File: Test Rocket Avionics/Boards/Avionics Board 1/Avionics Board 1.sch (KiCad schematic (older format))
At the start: 52 parts, among them J1 USB_A, J10 CHASSIS_GND, J11 CHASSIS_GND, J12 CHASSIS_GND, J13 CHASSIS_GND, J14 1S LiPo, J2 1S LiPo, J3 EXPANSION_HEADER, U1 ECS-.327-12.5-17X-TR, U2 SPX3819M5-L-3-3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

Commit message: Update some stuff
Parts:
- removed J3: EXPANSION_HEADER, Pin_Headers:Pin_Header_Straight_2x10_Pitch1.00mm, symbol Conn_02x11_Odd_Even
- added C20, C6: 2.2u, Capacitors_SMD:C_1206, symbol C
- added C21: 1u, Capacitors_SMD:C_0805, symbol C
- added C22: 220p, Capacitors_SMD:C_0805, symbol C
- added D6: D, Diodes_SMD:D_SOD-123F, symbol D
- added J3: EXPANSION_HEADER, Pin_Headers:Pin_Header_Straight_2x14_Pitch1.00mm, symbol Conn_02x12_Odd_Even
- added J4: USB_A, Connectors:USB_Mini-B, symbol USB_A
- added J5: SERVO, Pin_Headers:Pin_Header_Straight_1x03_Pitch2.54mm, symbol Conn_01x03
- added L1: 10u, Inductors_SMD:L_Wuerth_HCI-5040, symbol L
- added R10, R11, R17: 10k, Resistors_SMD:R_0805, symbol R
- added R18: 51k, Resistors_SMD:R_0805, symbol R
- added R19: 13.3k, Resistors_SMD:R_0805, symbol R
- added U10: NC7WZ07, TO_SOT_Packages_SMD:SOT-363_SC-70-6, symbol NC7WZ07
- added U11: LMR62014, TO_SOT_Packages_SMD:SOT-23-5, symbol LMR62014
- added U6: DS3231-SO16, Housings_SOIC:SOIC-16W_7.5x10.3mm_Pitch1.27mm, symbol DS3231-SO16
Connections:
- net labels added: 6V_SERVO_SUPPLY
- wire segments 139 -> 177
- no-connect marks 15 -> 27
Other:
- note added: "Place this USB on underside of the board"

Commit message: Connect JST connector to VBatt+ and GND nets
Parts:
- BZ1: symbol Buzzer -> Avionics-Board-1-rescue:Buzzer
- C1, C10, C11, C12, C13, C15, C16, C17, C18, C19, C2, C20, C21, C22, C3, C4, C5, C6, C7, C8, C9: symbol C -> Avionics-Board-1-rescue:C
- D1: symbol D_Schottky -> Avionics-Board-1-rescue:D_Schottky
- D2, D3, D4, D5: symbol LED -> Avionics-Board-1-rescue:LED
- D6: symbol D -> Avionics-Board-1-rescue:D
- J1, J4: symbol USB_A -> Avionics-Board-1-rescue:USB_A
- J10, J11, J12, J13: symbol Conn_01x01 -> Avionics-Board-1-rescue:Conn_01x01
- J14, J2: symbol Conn_01x02 -> Avionics-Board-1-rescue:Conn_01x02
- J3: symbol Conn_02x12_Odd_Even -> Avionics-Board-1-rescue:Conn_02x12_Odd_Even
- J5: symbol Conn_01x03 -> Avionics-Board-1-rescue:Conn_01x03
- L1: symbol L -> Avionics-Board-1-rescue:L
- R1, R10, R11, R12, R13, R14, R15, R16, R17, R18, R19, R2, R3, R4, R5, R6, R7, R8, R9: symbol R -> Avionics-Board-1-rescue:R
- U1, U8: symbol ECS-.327-12.5-17X-TR -> Avionics-Board-1-rescue:ECS-.327-12.5-17X-TR
- U10: symbol NC7WZ07 -> Avionics-Board-1-rescue:NC7WZ07
- U11: symbol LMR62014 -> Avionics-Board-1-rescue:LMR62014
- U2: symbol SPX3819M5-L-3-3 -> Avionics-Board-1-rescue:SPX3819M5-L-3-3
- U3: symbol ATSAMD21G18 -> Avionics-Board-1-rescue:ATSAMD21G18
- U4: symbol MCP73831 -> Avionics-Board-1-rescue:MCP73831
- U5: symbol MPL3115A2 -> Avionics-Board-1-rescue:MPL3115A2
- U6: symbol DS3231-SO16 -> Avionics-Board-1-rescue:DS3231-SO16
- U7: symbol BNO055 -> Avionics-Board-1-rescue:BNO055

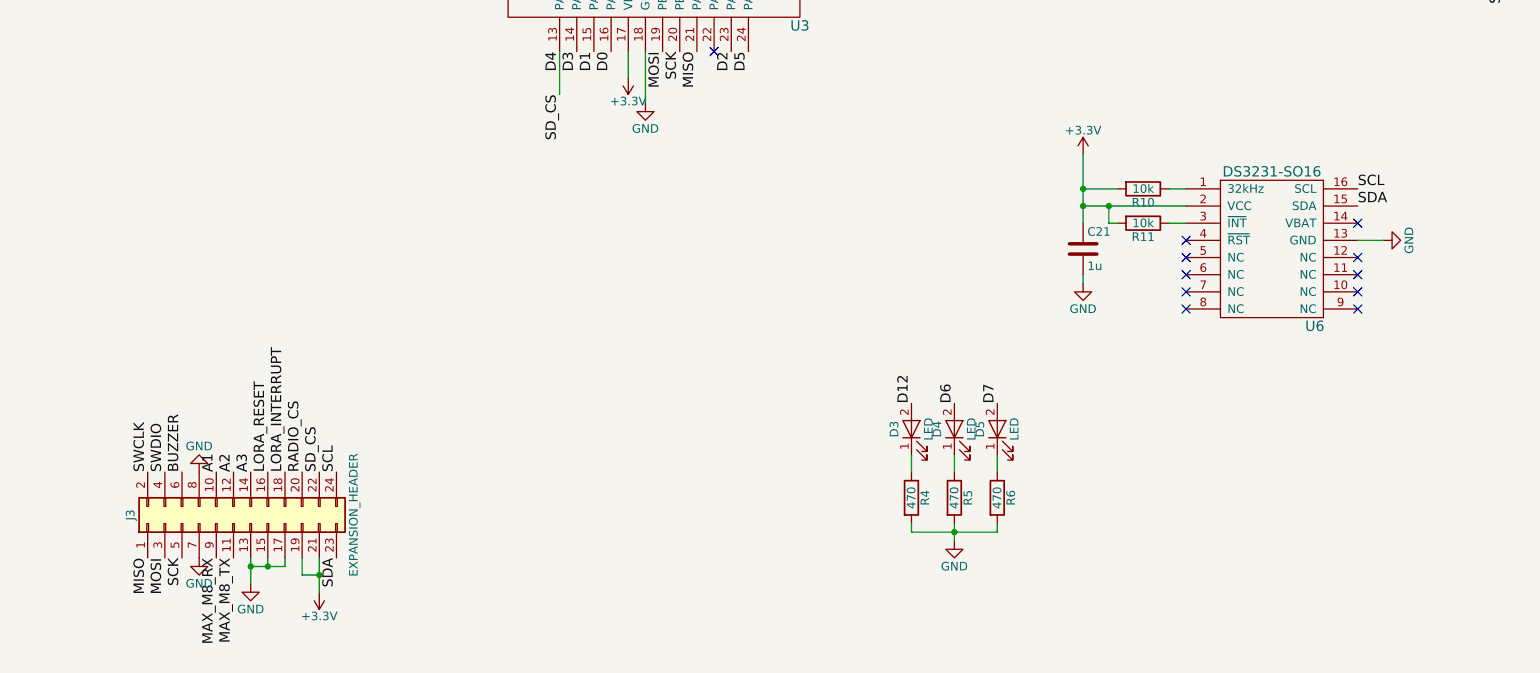
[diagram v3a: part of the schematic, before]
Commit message: Remove DS3231 and expand the J3 connector to include USB and improve pin ordering. Various bug fixes
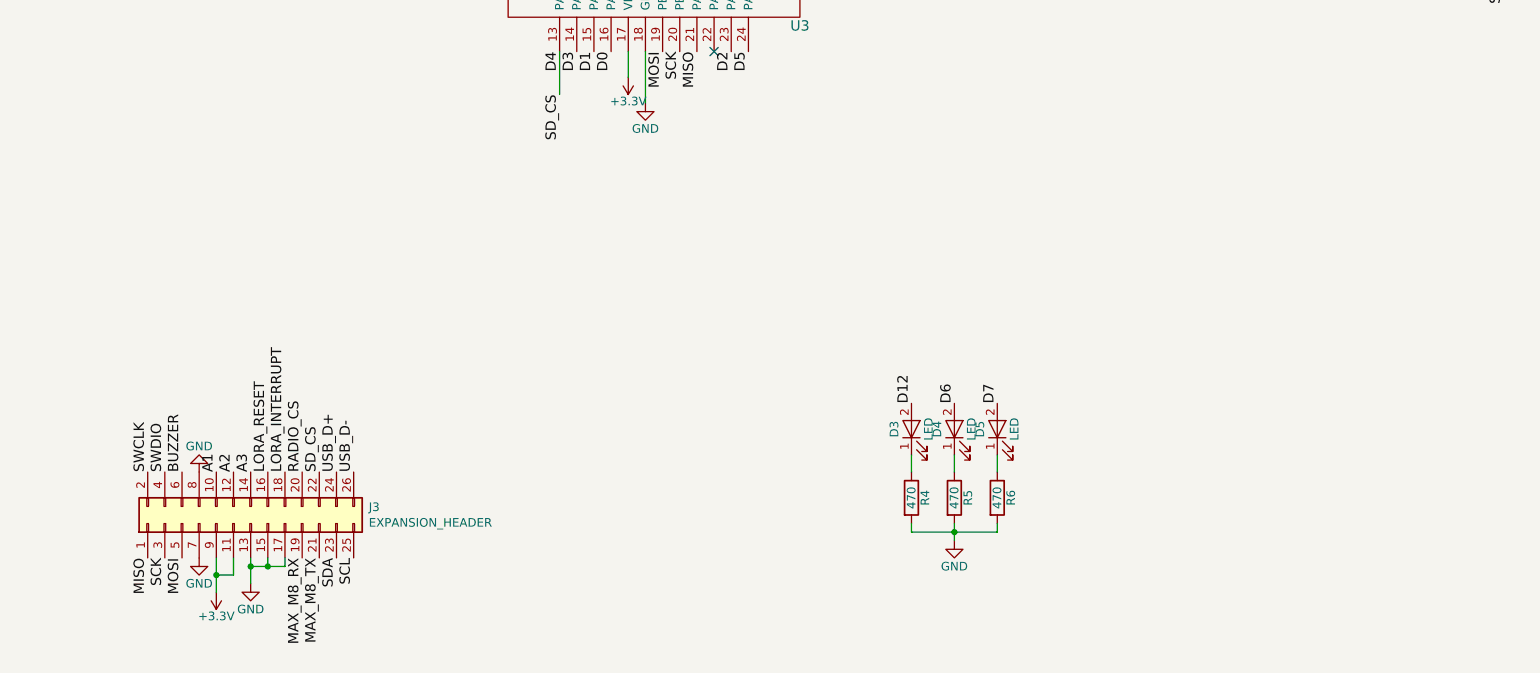
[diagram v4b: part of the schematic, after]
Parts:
- removed C21: 1u, Capacitors_SMD:C_0805, symbol Avionics-Board-1-rescue:C
- removed J3: EXPANSION_HEADER, Pin_Headers:Pin_Header_Straight_2x14_Pitch1.00mm, symbol Avionics-Board-1-rescue:Conn_02x12_Odd_Even
- removed R10, R11: 10k, Resistors_SMD:R_0805, symbol Avionics-Board-1-rescue:R
- removed U6: DS3231-SO16, Housings_SOIC:SOIC-16W_7.5x10.3mm_Pitch1.27mm, symbol Avionics-Board-1-rescue:DS3231-SO16
- added J3: EXPANSION_HEADER, Pin_Headers:Pin_Header_Straight_2x13_Pitch1.00mm, symbol Connector_Generic:Conn_02x13_Odd_Even
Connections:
- net +3V3: now also J3.11 (Pin_11), J3.9 (Pin_9)
- net A1: now also J3.10 (Pin_10)
- net A2: now also J3.12 (Pin_12)
- net A3: now also J3.14 (Pin_14)
- net A4: now also J3.16 (Pin_16)
- net A5: now also J3.6 (Pin_6)
- net D11: now also J3.21 (Pin_21)
- net D13: now also J3.19 (Pin_19)
- net D4: now also J3.22 (Pin_22)
- net D8: now also J3.18 (Pin_18)
- net D9: now also J3.20 (Pin_20)
- net GND: now also J3.13 (Pin_13), J3.15 (Pin_15), J3.17 (Pin_17), J3.7 (Pin_7), J3.8 (Pin_8)
- net MISO: now also J3.1 (Pin_1)
- net MOSI: now also J3.5 (Pin_5)
- net SCK: now also J3.3 (Pin_3)
- net SCL: now also J3.25 (Pin_25)
- net SDA: now also J3.23 (Pin_23)
- net SWCLK: now also J3.2 (Pin_2)
- net SWDIO: now also J3.4 (Pin_4)
- net USB_D+: now also J3.24 (Pin_24)
- net USB_D-: now also J3.26 (Pin_26)
- no-connect marks 27 -> 17
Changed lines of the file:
@@
 L Avionics-Board-1-rescue:+3.3V #PWR045
 U 1 1 5C4FAC8D
-P 2700 10150
-F 0 "#PWR045" H 2700 10000 50  0001 C CNN
-F 1 "+3.3V" H 2700 10290 50  0000 C CNN
-F 2 "" H 2700 10150 50  0001 C CNN
-F 3 "" H 2700 10150 50  0001 C CNN
-	1    2700 10150
+P 2100 10150
+F 0 "#PWR045" H 2100 10000 50  0001 C CNN
+F 1 "+3.3V" H 2100 10290 50  0000 C CNN
+F 2 "" H 2100 10150 50  0001 C CNN
+F 3 "" H 2100 10150 50  0001 C CNN
+	1    2100 10150
 	1    0    0    1
 $EndComp
+Text Label 1900 9950 3    60   ~ 0
+MOSI
 Text Label 1800 9950 3    60   ~ 0
-MOSI
-Text Label 1900 9950 3    60   ~ 0
 SCK
 Text Label 1700 9950 3    60   ~ 0
 MISO
-Text Label 2200 9950 3    60   ~ 0
+Text Label 2700 9950 3    60   ~ 0
 MAX_M8_TX
-Text Label 2100 9950 3    60   ~ 0
+Text Label 2600 9950 3    60   ~ 0
 MAX_M8_RX
 $Comp
@@
 SD_CS
 Wire Wire Line
-	2700 9950 2700 10050
-Wire Wire Line
-	2600 9950 2600 10050
-Wire Wire Line
-	2600 10050 2700 10050
-Connection ~ 2700 10050
-Wire Wire Line
 	2300 9950 2300 10000
 Wire Wire Line
@@
 	2500 10000 2500 9950
 Connection ~ 2400 10000
-$Comp
-L Avionics-Board-1-rescue:Conn_02x12_Odd_Even J3
-U 1 1 5C722513
-P 2200 9750
-F 0 "J3" H 2250 10350 50  0000 C CNN
-F 1 "EXPANSION_HEADER" H 2250 9050 50  0000 C CNN
-F 2 "Pin_Headers:Pin_Header_Straight_2x14_Pitch1.00mm" H 2200 9750 50  0001 C CNN
-F 3 "" H 2200 9750 50  0001 C CNN
-	1    2200 9750
-	0    -1   -1   0
-$EndComp
-Text Label 2800 9450 1    60   ~ 0
+Text Label 2900 9950 3    60   ~ 0
 SCL
 Text Label 2800 9950 3    60   ~ 0
@@
 	7100 5150 7200 5150
 Wire Wire Line
-	2700 10050 2700 10150
-Wire Wire Line
 	2300 10000 2300 10100
 Wire Wire Line
@@
 	10800 1800 10800 1850
 Wire Wire Line
-	7300 7900 7750 7900
-NoConn ~ 7750 8100
-NoConn ~ 7750 8200
-NoConn ~ 7750 8300
-NoConn ~ 7750 8400
-NoConn ~ 7750 8500
-NoConn ~ 8750 8500
-NoConn ~ 8750 8400
-NoConn ~ 8750 8300
-NoConn ~ 8750 8200
-NoConn ~ 8750 8000
-Wire Wire Line
-	8900 8100 8750 8100
-$Comp
-L Avionics-Board-1-rescue:GND #PWR063
-U 1 1 5C73A8EF
-P 8900 8100
-F 0 "#PWR063" H 8900 7850 50  0001 C CNN
-F 1 "GND" H 8900 7950 50  0000 C CNN
-F 2 "" H 8900 8100 50  0001 C CNN
-F 3 "" H 8900 8100 50  0001 C CNN
-	1    8900 8100
+	2100 10150 2100 10050
+Wire Wire Line
+	2200 9950 2200 10050
+Wire Wire Line
+	2200 10050 2100 10050
+Connection ~ 2100 10050
+Wire Wire Line
+	2100 10050 2100 9950
+$Comp
+L Connector_Generic:Conn_02x13_Odd_Even J3
+U 1 1 5CB1EFA8
+P 2300 9750
+F 0 "J3" V 2396 9062 50  0000 R CNN
+F 1 "EXPANSION_HEADER" V 2305 9062 50  0000 R CNN
+F 2 "Pin_Headers:Pin_Header_Straight_2x13_Pitch1.00mm" H 2300 9750 50  0001 C CNN
+F 3 "~" H 2300 9750 50  0001 C CNN
+	1    2300 9750
 	0    -1   -1   0
 $EndComp
-Text Label 8750 7800 0    60   ~ 0
-SCL
-Text Label 8750 7900 0    60   ~ 0
-SDA
-Wire Wire Line
-	7150 8350 7150 8300
-$Comp
-L Avionics-Board-1-rescue:GND #PWR062
-U 1 1 5C739AF9
-P 7150 8350
-F 0 "#PWR062" H 7150 8100 50  0001 C CNN
-F 1 "GND" H 7150 8200 50  0000 C CNN
-F 2 "" H 7150 8350 50  0001 C CNN
-F 3 "" H 7150 8350 50  0001 C CNN
-	1    7150 8350
-	1    0    0    -1
-$EndComp
-$Comp
-L Avionics-Board-1-rescue:C C21
-U 1 1 5C73906A
-P 7150 8150
-F 0 "C21" H 7175 8250 50  0000 L CNN
-F 1 "1u" H 7175 8050 50  0000 L CNN
-F 2 "Capacitors_SMD:C_0805" H 7188 8000 50  0001 C CNN
-F 3 "" H 7150 8150 50  0001 C CNN
-	1    7150 8150
-	1    0    0    -1
-$EndComp
-Wire Wire Line
-	7150 7800 7350 7800
-Connection ~ 7150 7800
-Wire Wire Line
-	7150 7600 7150 7800
-$Comp
-L Avionics-Board-1-rescue:+3.3V #PWR061
-U 1 1 5C738EB5
-P 7150 7600
-F 0 "#PWR061" H 7150 7450 50  0001 C CNN
-F 1 "+3.3V" H 7150 7740 50  0000 C CNN
-F 2 "" H 7150 7600 50  0001 C CNN
-F 3 "" H 7150 7600 50  0001 C CNN
-	1    7150 7600
-	1    0    0    -1
-$EndComp
-Wire Wire Line
-	7300 8000 7300 7900
-Wire Wire Line
-	7350 8000 7300 8000
-Connection ~ 7300 7900
-Wire Wire Line
-	7150 7800 7150 7900
-Wire Wire Line
-	7150 7900 7150 8000
-Connection ~ 7150 7900
-Wire Wire Line
-	7150 7900 7300 7900
-Wire Wire Line
-	7650 8000 7750 8000
-Wire Wire Line
-	7650 7800 7750 7800
-$Comp
-L Avionics-Board-1-rescue:R R11
-U 1 1 5C738866
-P 7500 8000
-F 0 "R11" V 7580 8000 50  0000 C CNN
-F 1 "10k" V 7500 8000 50  0000 C CNN
-F 2 "Resistors_SMD:R_0805" V 7430 8000 50  0001 C CNN
-F 3 "" H 7500 8000 50  0001 C CNN
-	1    7500 8000
-	0    1    1    0
-$EndComp
-$Comp
-L Avionics-Board-1-rescue:R R10
-U 1 1 5C738747
-P 7500 7800
-F 0 "R10" V 7580 7800 50  0000 C CNN
-F 1 "10k" V 7500 7800 50  0000 C CNN
-F 2 "Resistors_SMD:R_0805" V 7430 7800 50  0001 C CNN
-F 3 "" H 7500 7800 50  0001 C CNN
-	1    7500 7800
-	0    1    1    0
-$EndComp
-$Comp
-L Avionics-Board-1-rescue:DS3231-SO16 U6
-U 1 1 5C7360A0
-P 8250 8150
-F 0 "U6" H 8500 7700 60  0000 C CNN
-F 1 "DS3231-SO16" H 8250 8600 60  0000 C CNN
-F 2 "Housings_SOIC:SOIC-16W_7.5x10.3mm_Pitch1.27mm" H 8250 7450 60  0001 C CNN
-F 3 "" H 8250 7450 60  0001 C CNN
-	1    8250 8150
-	1    0    0    -1
-$EndComp
+Text Label 2800 9450 1    60   ~ 0
+USB_D+
+Text Label 2900 9450 1    60   ~ 0
+USB_D-
 $EndSCHEMATC

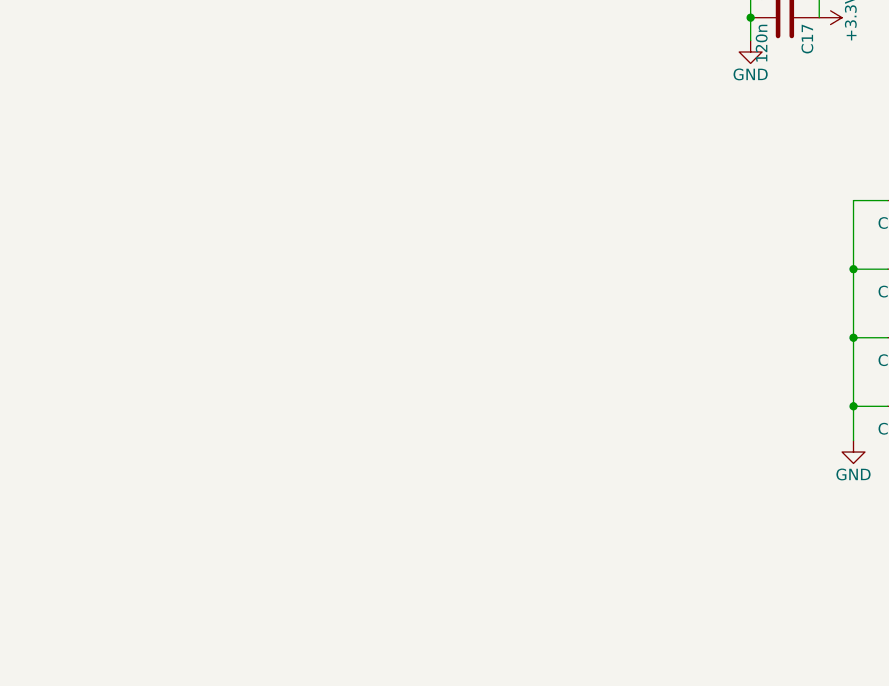
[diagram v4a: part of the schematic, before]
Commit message: Add micro SD Card, clean up ref des, power 6v boost directly from battery instead of 3.3V rail
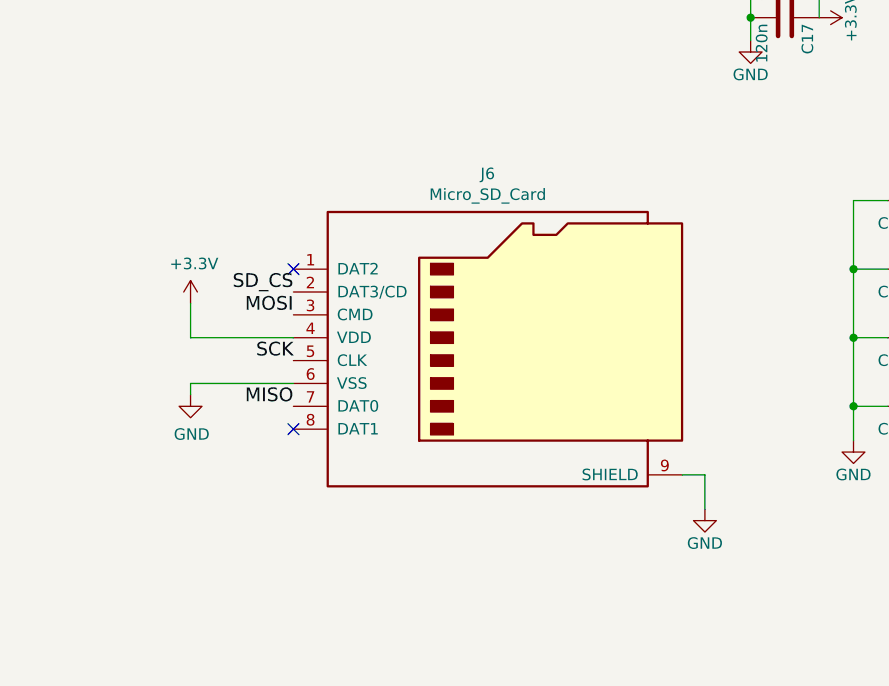
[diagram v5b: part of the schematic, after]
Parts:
- added J6: Micro_SD_Card, DannysLib:MicroSD_DM3D-SF, symbol Connector:Micro_SD_Card
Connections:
- net +3V3: now also J6.4 (VDD)
- net D4: now also J6.2 (DAT3/CD)
- net GND: now also J6.6 (VSS), J6.9 (SHIELD)
- net MISO: now also J6.7 (DAT0)
- net MOSI: now also J6.3 (CMD)
- net SCK: now also J6.5 (CLK)
- no-connect marks 17 -> 19
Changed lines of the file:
@@
 Text Label 2900 9450 1    60   ~ 0
 USB_D-
+$Comp
+L Connector:Micro_SD_Card J6
+U 1 1 5CC9B146
+P 9000 9100
+F 0 "J6" H 8950 9817 50  0000 C CNN
+F 1 "Micro_SD_Card" H 8950 9726 50  0000 C CNN
+F 2 "DannysLib:MicroSD_DM3D-SF" H 10150 9400 50  0001 C CNN
+F 3 "http://katalog.we-online.de/em/datasheet/693072010801.pdf" H 9000 9100 50  0001 C CNN
+	1    9000 9100
+	1    0    0    -1
+$EndComp
+NoConn ~ 8100 8800
+NoConn ~ 8100 9500
+Text Label 8100 9400 2    60   ~ 0
+MISO
+Text Label 8100 9000 2    60   ~ 0
+MOSI
+Text Label 8100 8900 2    60   ~ 0
+SD_CS
+Text Label 8100 9200 2    60   ~ 0
+SCK
+$Comp
+L Avionics-Board-1-rescue:+3.3V #PWR061
+U 1 1 5CCC4D2C
+P 7650 8950
+F 0 "#PWR061" H 7650 8800 50  0001 C CNN
+F 1 "+3.3V" H 7665 9123 50  0000 C CNN
+F 2 "" H 7650 8950 50  0001 C CNN
+F 3 "" H 7650 8950 50  0001 C CNN
+	1    7650 8950
+	1    0    0    -1
+$EndComp
+Wire Wire Line
+	7650 8950 7650 9100
+Wire Wire Line
+	7650 9100 8100 9100
+$Comp
+L Avionics-Board-1-rescue:GND #PWR062
+U 1 1 5CCD1F6F
+P 7650 9350
+F 0 "#PWR062" H 7650 9100 50  0001 C CNN
+F 1 "GND" H 7655 9177 50  0000 C CNN
+F 2 "" H 7650 9350 50  0001 C CNN
+F 3 "" H 7650 9350 50  0001 C CNN
+	1    7650 9350
+	1    0    0    -1
+$EndComp
+Wire Wire Line
+	7650 9350 7650 9300
+Wire Wire Line
+	7650 9300 8100 9300
+$Comp
+L Avionics-Board-1-rescue:GND #PWR?
+U 1 1 5CCE34EA
+P 9900 9850
+F 0 "#PWR?" H 9900 9600 50  0001 C CNN
+F 1 "GND" H 9900 9700 50  0000 C CNN
+F 2 "" H 9900 9850 50  0001 C CNN
+F 3 "" H 9900 9850 50  0001 C CNN
+	1    9900 9850
+	1    0    0    -1
+$EndComp
+Wire Wire Line
+	9900 9700 9800 9700
+Wire Wire Line
+	9900 9700 9900 9850
 $EndSCHEMATC

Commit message: Add LMS303C and BMP280
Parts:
- removed C18, C19: 22p, Capacitors_SMD:C_0805, symbol Avionics-Board-1-rescue:C
- removed U8: ECS-.327-12.5-17X-TR, DannysLib:XC1195CT-ND, symbol Avionics-Board-1-rescue:ECS-.327-12.5-17X-TR
- added C14, C23: 100n, Capacitors_SMD:C_0805, symbol Avionics-Board-1-rescue:C
- added C24: 10u, Capacitors_SMD:C_1206, symbol Avionics-Board-1-rescue:C
- added U6: LSM303C, Housings_LGA:LGA-12_2x2mm_Pitch0.5mm, symbol Danny's_Lib:LSM303C
- added U8: BMP280, DannysLib:BMP280, symbol Danny's_Lib:BMP280
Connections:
- net +3V3: now also C23.2, C24.2, U6.10 (VDD_IO), U6.2 (CS_XL), U6.3 (CS_MAG), U6.9 (VDD), U8.2 (CSB), U8.8 (VDD); no longer C20.1, L1.2, R17.1, U11.5 (VIN)
- net +BATT: now also C20.1, L1.2, R17.1, U11.5 (VIN)
- net GND: now also C14.2, C23.1, C24.1, U6.6 (GND), U6.8 (GND), U8.1 (GND), U8.5 (ADDR), U8.6 (VDDIO), U8.7 (GND)
- net SCL: now also U6.1 (SCL), U8.4 (SCL)
- net SDA: now also U6.4 (SDA), U8.3 (SDA)
- new net: C14.1, U6.5 (C1)
- no-connect marks 19 -> 22
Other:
- note added: "Capacitors omitted for manufacturing ease"
